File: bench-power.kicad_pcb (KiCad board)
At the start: 2 copper layers, 39 x 76 mm, 35 parts, among them J1 PWR_OUT, J2 POWER_IN_BRD, J3 LOAD

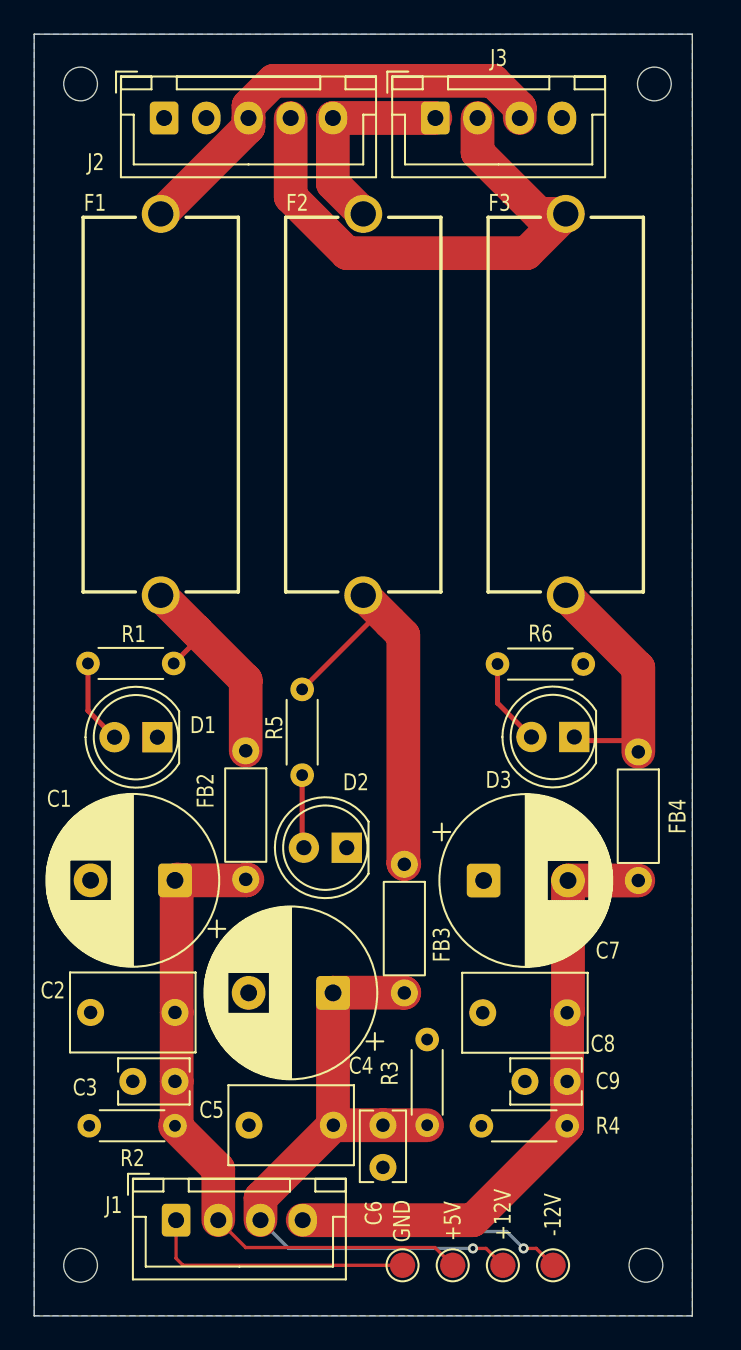
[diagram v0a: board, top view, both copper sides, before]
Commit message: shuffle jst connectors
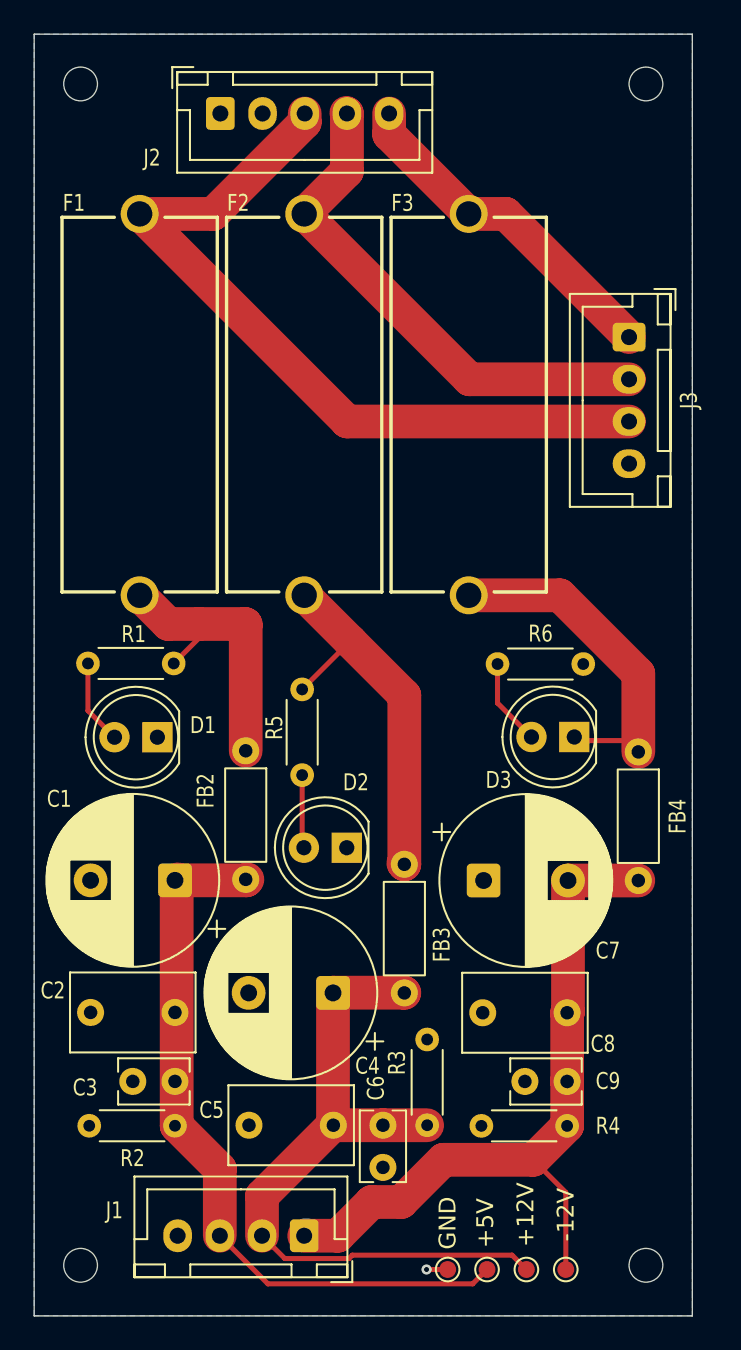
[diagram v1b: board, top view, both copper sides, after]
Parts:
- TP1, TP2, TP3, TP4: footprint TestPoint:TestPoint_Pad_D1.5mm -> TestPoint:TestPoint_Pad_D1.0mm
- moved J3 17.3 mm to (175.2, 66.0), turned to -90 degrees
- moved J1 7.65 mm to (156.0, 119.2), turned to 180 degrees
- moved F3 5.75 mm to (165.8, 70.0)
- moved F2 3.50 mm to (156.0, 70.0)
- moved J2 3.34 mm to (151.0, 52.8)
- moved TP1 2.68 mm to (164.5, 121.2)
- moved TP2 2.05 mm to (166.8, 121.2)
- moved TP3 1.42 mm to (169.2, 121.2)
- moved F1 1.25 mm to (146.2, 70.0)
- moved TP4 0.79 mm to (171.5, 121.2)
- moved REF** 0.50 mm to (176.2, 51.0)
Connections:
- C1 pad 1: Net-(J1-Pin_2) -> Net-(J1-Pin_3)
- C2 pad 2: Net-(J1-Pin_2) -> Net-(J1-Pin_3)
- C3 pad 2: Net-(J1-Pin_2) -> Net-(J1-Pin_3)
- C4 pad 1: Net-(J1-Pin_3) -> Net-(J1-Pin_2)
- C5 pad 2: Net-(J1-Pin_3) -> Net-(J1-Pin_2)
- C6 pad 2: Net-(J1-Pin_3) -> Net-(J1-Pin_2)
- C7 pad 2: Net-(J1-Pin_4) -> Net-(J1-Pin_1)
- C8 pad 2: Net-(J1-Pin_4) -> Net-(J1-Pin_1)
- C9 pad 2: Net-(J1-Pin_4) -> Net-(J1-Pin_1)
- FB2 pad 2: Net-(J1-Pin_2) -> Net-(J1-Pin_3)
- FB3 pad 2: Net-(J1-Pin_3) -> Net-(J1-Pin_2)
- FB4 pad 2: Net-(J1-Pin_4) -> Net-(J1-Pin_1)
- J1 pad 1: GND -> Net-(J1-Pin_1)
- J1 pad 4: Net-(J1-Pin_4) -> GND
- J2 pad 4: /-Vout -> /+Vout
- J2 pad 5: /+Vout -> /-Vout
- J3 pad 1: /+Vout -> /-Vout
- J3 pad 2: /-Vout -> /+Vout
- R2 pad 2: Net-(J1-Pin_2) -> Net-(J1-Pin_3)
- R3 pad 2: Net-(J1-Pin_3) -> Net-(J1-Pin_2)
- R4 pad 2: Net-(J1-Pin_4) -> Net-(J1-Pin_1)
- TP2 pad 1: Net-(J1-Pin_2) -> Net-(J1-Pin_3)
- TP3 pad 1: Net-(J1-Pin_3) -> Net-(J1-Pin_2)
- TP4 pad 1: Net-(J1-Pin_4) -> Net-(J1-Pin_1)
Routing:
- net Net-(J1-Pin_4): track 52.7 -> 0.00 mm, vias 1 -> 0
- net Net-(J1-Pin_1): track 0.00 -> 44.7 mm
- net /+5Vout: track 26.8 -> 46.6 mm
- net /+Vout: track 12.5 -> 30.4 mm
- net GND: track 15.9 -> 1.25 mm, vias 0 -> 1
- net /-Vout: track 32.1 -> 20.4 mm
- net -12V: track 15.2 -> 20.8 mm
- net +5V: track 13.8 -> 17.4 mm
- net Net-(J1-Pin_3): track 40.5 -> 43.8 mm, vias 1 -> 0
- net Net-(J1-Pin_2): track 40.5 -> 43.4 mm
- net +12V: track 23.8 -> 22.5 mm
